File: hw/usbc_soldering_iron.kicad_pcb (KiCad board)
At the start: 4 copper layers, 100 x 13.5 mm, 91 parts, among them J1 U263-163N-4OS1735, J10 Conn_01x01, J11 Conn_01x01, J12 Conn_01x01, J13 Conn_01x01, J14 Conn_01x01, J15 Conn_01x01, J16 Conn_01x01, J17 Conn_01x01, J18 Conn_01x01, J19 Conn_01x01, J2 Conn_01x01, J20 Conn_01x01, J21 Conn_01x01, J22 Conn_01x01, J3 OLED, J4 Conn_01x01, J5 Conn_01x01, J6 Conn_01x01, J7 Conn_01x01, J8 Conn_01x01, J9 Conn_01x01, Q1 AGM403AP, SW1 SW_Push, U1 SC7A20, U10 TPA191Ax, U2 CH32X035F8U6, U3 TPD4E05U06DQA, U4 SIQ-02FVS3, U5 AP63203WU, U6 TLV333IDBVR, U8 MT3608, U9 IRS20752L, IRS20752L, NSG10752

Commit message: display
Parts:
- moved C14 12.9 mm to (116.7, 73.1), turned to 0 degrees
- moved J22 11.6 mm to (120.4, 78.5), turned to 0 degrees
- moved J19 9.21 mm to (118.9, 78.5), turned to 0 degrees
- moved C16 9.16 mm to (119.8, 73.1), turned to 0 degrees
- moved C20 7.42 mm to (116.7, 74.6), turned to 0 degrees
- moved J20 7.33 mm to (117.4, 78.5), turned to 0 degrees
- moved C18 7.28 mm to (116.7, 71.6)
- moved C22 7.18 mm to (116.7, 76.1), turned to 0 degrees
- moved J21 6.36 mm to (115.9, 78.5), turned to 0 degrees
- moved C17 5.81 mm to (119.8, 71.6), turned to 0 degrees
- moved R13 5.49 mm to (119.8, 76.1), turned to 0 degrees
- moved R12 4.86 mm to (119.8, 74.6)
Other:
- board size 100 x 13.5 mm -> 100 x 36.8 mm

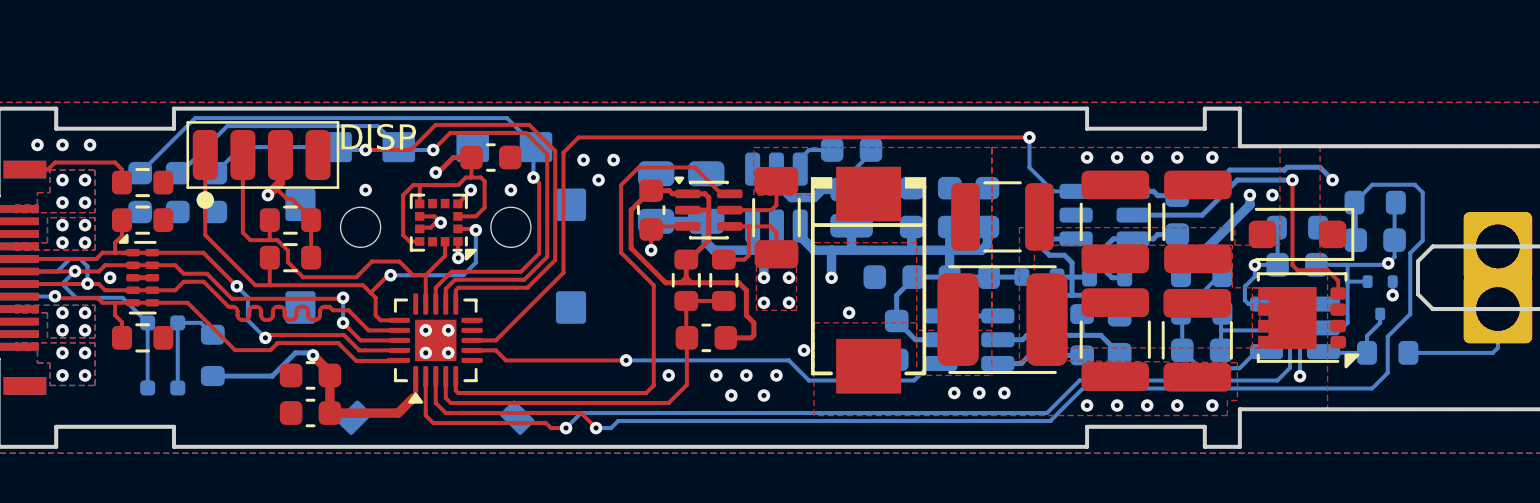
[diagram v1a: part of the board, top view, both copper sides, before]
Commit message: tlv333 rc filter
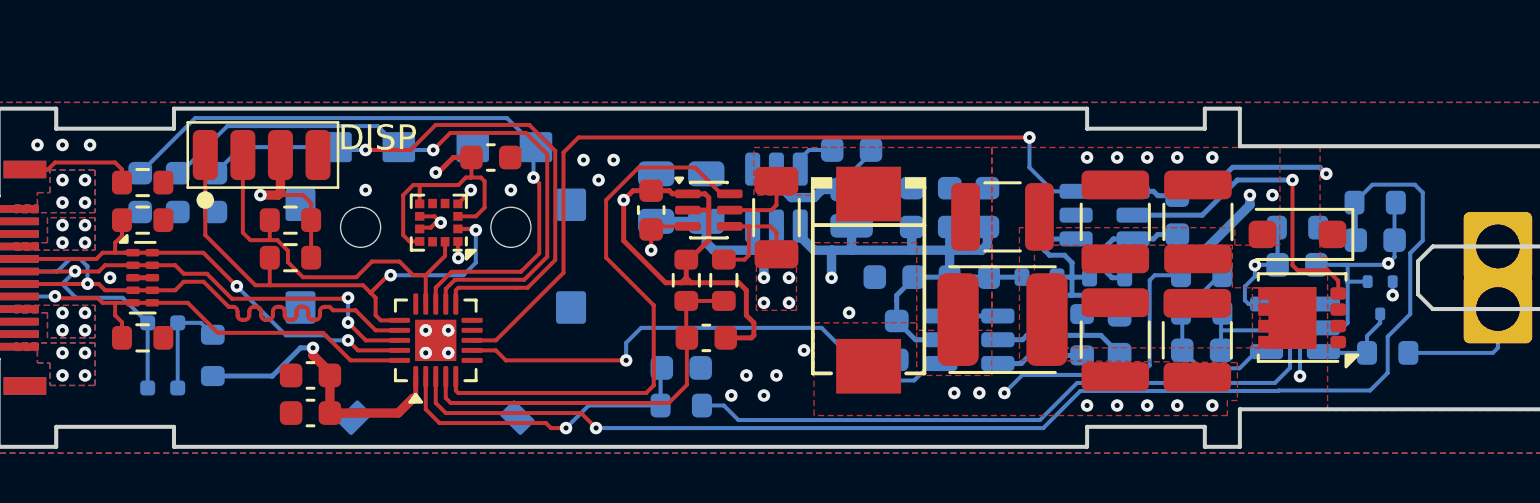
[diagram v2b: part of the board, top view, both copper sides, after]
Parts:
- added C33: TBD, Capacitor_SMD:C_0603_1608Metric, B.Cu at (132.7, 103.6)
- added R20: TBD, Resistor_SMD:R_0603_1608Metric, B.Cu at (132.7, 105.1)
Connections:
- C10 pad 2: /TC_FB -> Net-(C10-Pad2)
- R10 pad 2: /TC_FB -> Net-(C10-Pad2)
- U2 pad 9: /DISP_NRST -> /NRST
- U6 pad 1: /TC_FB -> Net-(C10-Pad2)
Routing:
- net Net-(C10-Pad2): track 0.00 -> 32.5 mm
- net /TC_FB: track 45.1 -> 12.9 mm
- net GND: track 45.4 -> 57.9 mm, vias 49 -> 48
- net +3.3V: track 112.6 -> 114.3 mm
- net /VDRIVE_ON: track 19.5 -> 21.0 mm
- net /CC1: track 19.3 -> 18.7 mm

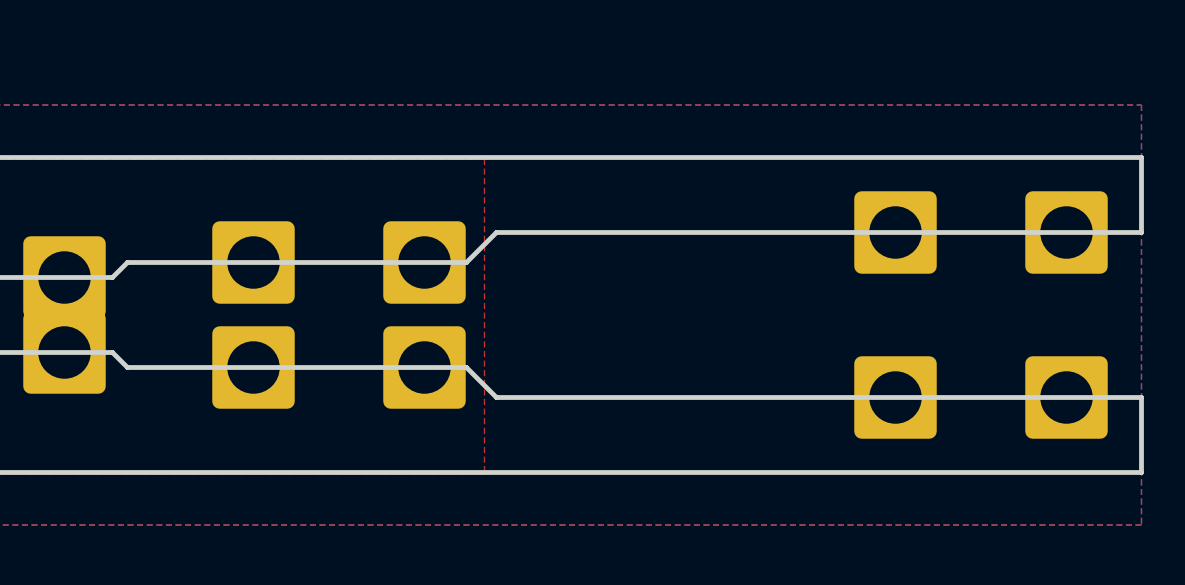
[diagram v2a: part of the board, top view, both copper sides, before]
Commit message: vias around tip contacts
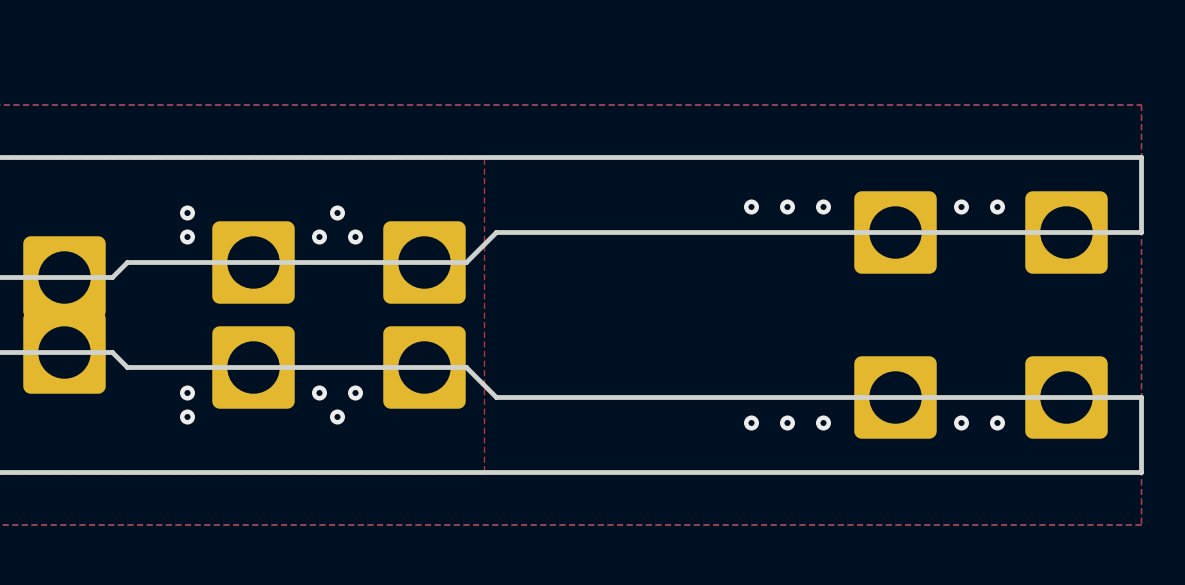
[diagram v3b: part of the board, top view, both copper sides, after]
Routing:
- net GND: vias 48 -> 58
- net /BLUE: vias 1 -> 11
- added copper zone on In1.Cu, net /BLUE
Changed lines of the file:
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@@
 	)
 	(via
+		(at 199 103.6)
+		(size 0.5)
+		(drill 0.2)
+		(layers "F.Cu" "B.Cu")
+		(free yes)
+		(net "GND")
+	)
+	(via
 		(at 151.3 95.2)
 		(size 0.5)
@@
 	)
 	(via
+		(at 192 103.6)
+		(size 0.5)
+		(drill 0.2)
+		(layers "F.Cu" "B.Cu")
+		(free yes)
+		(net "GND")
+	)
+	(via
 		(at 136 104.7)
 		(size 0.5)
@@
 	)
 	(via
+		(at 200.2 103.6)
+		(size 0.5)
+		(drill 0.2)
+		(layers "F.Cu" "B.Cu")
+		(free yes)
+		(net "GND")
+	)
+	(via
 		(at 144.6 104.6)
 		(size 0.5)
@@
 	)
 	(via
+		(at 199 96.4)
+		(size 0.5)
+		(drill 0.2)
+		(layers "F.Cu" "B.Cu")
+		(free yes)
+		(net "GND")
+	)
+	(via
 		(at 128.8 95.3)
 		(size 0.5)
@@
 	)
 	(via
+		(at 194.4 103.6)
+		(size 0.5)
+		(drill 0.2)
+		(layers "F.Cu" "B.Cu")
+		(free yes)
+		(net "GND")
+	)
+	(via
 		(at 145.6 104.6)
 		(size 0.5)
@@
 	)
 	(via
+		(at 193.2 103.6)
+		(size 0.5)
+		(drill 0.2)
+		(layers "F.Cu" "B.Cu")
+		(free yes)
+		(net "GND")
+	)
+	(via
 		(at 108.9 96.1)
 		(size 0.5)
@@
 	)
 	(via
+		(at 200.2 96.4)
+		(size 0.5)
+		(drill 0.2)
+		(layers "F.Cu" "B.Cu")
+		(free yes)
+		(net "GND")
+	)
+	(via
 		(at 123.4 103)
 		(size 0.5)
@@
 	)
 	(via
+		(at 193.2 96.4)
+		(size 0.5)
+		(drill 0.2)
+		(layers "F.Cu" "B.Cu")
+		(free yes)
+		(net "GND")
+	)
+	(via
 		(at 108.9 103.9)
 		(size 0.5)
@@
 	)
 	(via
+		(at 194.4 96.4)
+		(size 0.5)
+		(drill 0.2)
+		(layers "F.Cu" "B.Cu")
+		(free yes)
+		(net "GND")
+	)
+	(via
+		(at 192 96.4)
+		(size 0.5)
+		(drill 0.2)
+		(layers "F.Cu" "B.Cu")
+		(free yes)
+		(net "GND")
+	)
+	(via
 		(at 153.9 105.1)
 		(size 0.5)
@@
 		(net "/BLUE")
 	)
+	(via
+		(at 173.2 103.4)
+		(size 0.5)
+		(drill 0.2)
+		(layers "F.Cu" "B.Cu")
+		(free yes)
+		(net "/BLUE")
+	)
+	(via
+		(at 177.6 102.6)
+		(size 0.5)
+		(drill 0.2)
+		(layers "F.Cu" "B.Cu")
+		(free yes)
+		(net "/BLUE")
+	)
+	(via
+		(at 173.2 102.6)
+		(size 0.5)
+		(drill 0.2)
+		(layers "F.Cu" "B.Cu")
+		(free yes)
+		(net "/BLUE")
+	)
+	(via
+		(at 173.2 97.4)
+		(size 0.5)
+		(drill 0.2)
+		(layers "F.Cu" "B.Cu")
+		(free yes)
+		(net "/BLUE")
+	)
+	(via
+		(at 177.6 97.4)
+		(size 0.5)
+		(drill 0.2)
+		(layers "F.Cu" "B.Cu")
+		(free yes)
+		(net "/BLUE")
+	)
+	(via
+		(at 178.8 97.4)
+		(size 0.5)
+		(drill 0.2)
+		(layers "F.Cu" "B.Cu")
+		(free yes)
+		(net "/BLUE")
+	)
+	(via
+		(at 173.2 96.6)
+		(size 0.5)
+		(drill 0.2)
+		(layers "F.Cu" "B.Cu")
+		(free yes)
+		(net "/BLUE")
+	)
+	(via
+		(at 178.8 102.6)
+		(size 0.5)
+		(drill 0.2)
+		(layers "F.Cu" "B.Cu")
+		(free yes)
+		(net "/BLUE")
+	)
+	(via
+		(at 178.2 103.4)
+		(size 0.5)
+		(drill 0.2)
+		(layers "F.Cu" "B.Cu")
+		(free yes)
+		(net "/BLUE")
+	)
+	(via
+		(at 178.2 96.6)
+		(size 0.5)
+		(drill 0.2)
+		(layers "F.Cu" "B.Cu")
+		(free yes)
+		(net "/BLUE")
+	)
 	(segment
 		(start 158.19 95.59)
@@
 			)
 		)
+	)
+	(zone
+		(net "/BLUE")
+		(layer "In1.Cu")
+		(hatch edge 0.5)
+		(priority 11)
+		(connect_pads
+			(clearance 0.2)
+		)
+		(min_thickness 0.25)
+		(fill yes
+			(thermal_gap 0.3)
+			(thermal_bridge_width 1)
+			(island_removal_mode 0)
+		)
+		(polygon
+			(pts
+				(xy 172.6 95.6) (xy 182.4 95.6) (xy 182.4 104.4) (xy 172.6 104.4)
+			)
+		)

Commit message: oled board
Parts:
- added H1: MountingHole, MountingHole:MountingHole_2.2mm_M2_ISO7380, F.Cu at (114.6, 87.3)
- added H2: MountingHole, MountingHole:MountingHole_2.2mm_M2_ISO7380, F.Cu at (145.7, 87.3)
- J3: footprint Custom:FPC_14 -> Custom:X069-9616TSWIG02-H14
- moved C17 18.6 mm to (130.8, 86.7)
- moved C14 17.4 mm to (127.7, 86.7)
- moved C18 17.4 mm to (127.7, 85.2)
- moved C20 17.4 mm to (127.7, 88.2)
- moved C22 17.4 mm to (127.7, 89.7)
- moved R12 17.4 mm to (130.8, 88.2)
- moved R13 17.4 mm to (130.8, 89.7)
- moved J3 16.7 mm to (124.8, 87.4), turned to 180 degrees
- moved C16 16.3 mm to (130.8, 85.2)
- moved J19 13.0 mm to (123.7, 90.7)
- moved J20 13.0 mm to (122.2, 90.7)
- moved J21 13.0 mm to (120.7, 90.7)
- moved J22 13.0 mm to (125.2, 90.7)
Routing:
- net /DISP_VCC: track 0.00 -> 23.9 mm, vias 0 -> 2
- net Net-(J3-Pin_14): track 0.00 -> 19.0 mm, vias 0 -> 1
- net Net-(J3-Pin_13): track 0.00 -> 14.3 mm, vias 0 -> 1
- net Net-(J3-Pin_12): track 0.00 -> 14.1 mm, vias 0 -> 1
- net /DISP_NRST: track 0.00 -> 12.7 mm, vias 0 -> 1
- net Net-(J3-Pin_3): track 0.00 -> 11.3 mm, vias 0 -> 1
- net Net-(J3-Pin_1): track 0.00 -> 10.9 mm, vias 0 -> 1
- net /DISP_GND: track 0.00 -> 8.63 mm, vias 0 -> 7
- net Net-(J3-Pin_2): track 0.00 -> 6.97 mm, vias 0 -> 1
- net Net-(J3-Pin_4): track 0.00 -> 6.80 mm, vias 0 -> 1
- net /DISP_SDA: track 0.00 -> 5.13 mm, vias 0 -> 1
- net /DISP_SCL: track 0.00 -> 3.42 mm, vias 0 -> 1
- net +3.3V: track 114.3 -> 114.9 mm
- added copper zone on B.Cu, net /DISP_GND
- added copper zone on F.Cu, net /DISP_GND
- added copper zone on In1.Cu, net /DISP_GND
- added copper zone on In2.Cu, net /DISP_GND
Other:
- board size 100 x 36.8 mm -> 100 x 24 mm

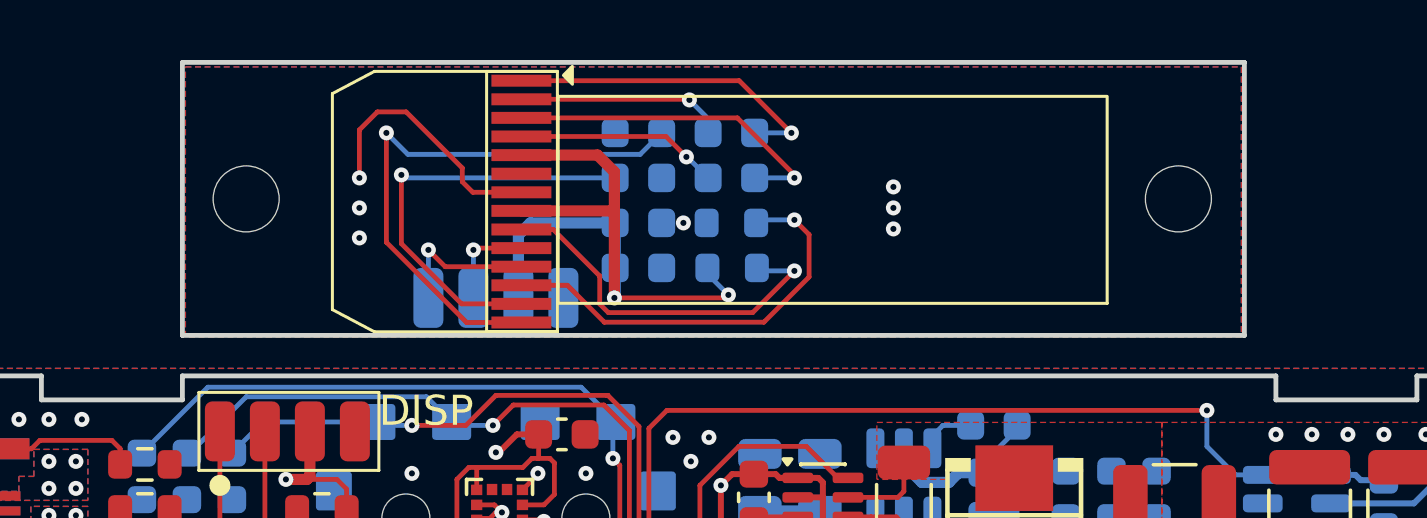
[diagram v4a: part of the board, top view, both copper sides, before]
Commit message: removed oled from main board
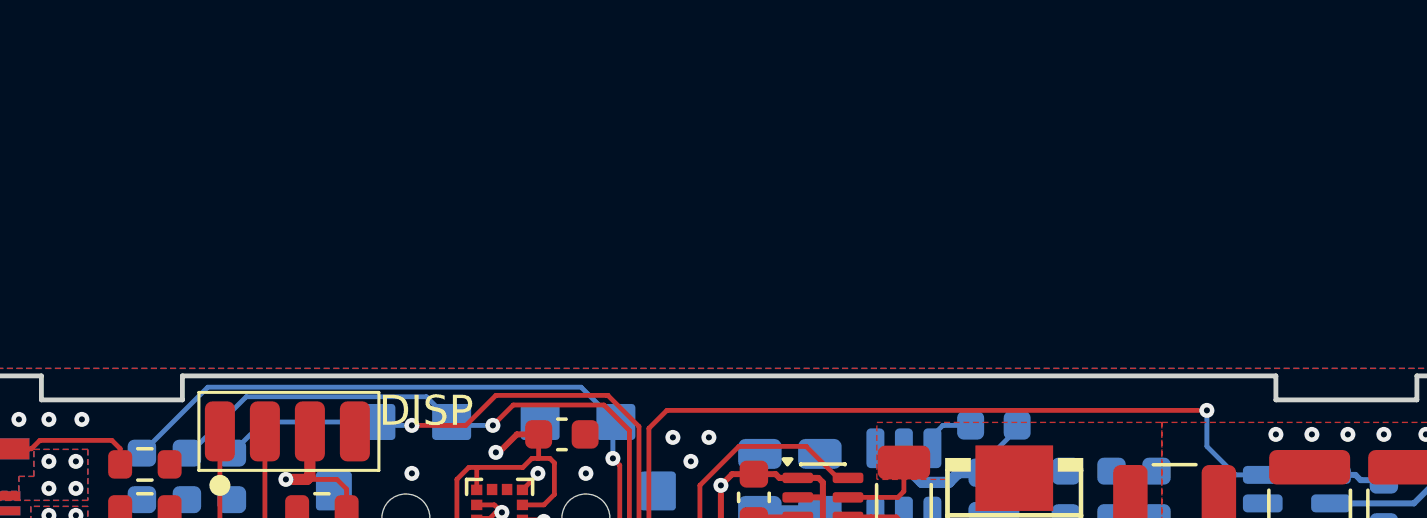
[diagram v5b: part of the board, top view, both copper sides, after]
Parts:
- removed C14, C20: 4.7u, Capacitor_SMD:C_0603_1608Metric
- removed C16, C17: 1u, Capacitor_SMD:C_0603_1608Metric
- removed C18, C22: 100n, Capacitor_SMD:C_0603_1608Metric
- removed H1, H2: MountingHole, MountingHole:MountingHole_2.2mm_M2_ISO7380
- removed J19, J20, J21, J22: Conn_01x01, Connector_Wire:SolderWirePad_1x01_SMD_1x2mm
- removed J3: OLED, Custom:X069-9616TSWIG02-H14
- removed R12: 560k, Resistor_SMD:R_0603_1608Metric
- removed R13: 1k, Resistor_SMD:R_0603_1608Metric
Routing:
- net /DISP_VCC: track 23.9 -> 0.00 mm, vias 2 -> 0
- net Net-(J3-Pin_14): track 19.0 -> 0.00 mm, vias 1 -> 0
- net Net-(J3-Pin_13): track 14.3 -> 0.00 mm, vias 1 -> 0
- net Net-(J3-Pin_12): track 14.1 -> 0.00 mm, vias 1 -> 0
- net /DISP_NRST: track 12.7 -> 0.00 mm, vias 1 -> 0
- net Net-(J3-Pin_3): track 11.3 -> 0.00 mm, vias 1 -> 0
- net Net-(J3-Pin_1): track 10.9 -> 0.00 mm, vias 1 -> 0
- net /DISP_GND: track 8.63 -> 0.00 mm, vias 7 -> 0
- net Net-(J3-Pin_2): track 6.97 -> 0.00 mm, vias 1 -> 0
- net Net-(J3-Pin_4): track 6.80 -> 0.00 mm, vias 1 -> 0
- net /DISP_SDA: track 5.13 -> 0.00 mm, vias 1 -> 0
- net /DISP_SCL: track 3.42 -> 0.00 mm, vias 1 -> 0
- removed copper zone on B.Cu, net /DISP_GND
- removed copper zone on F.Cu, net /DISP_GND
- removed copper zone on In1.Cu, net /DISP_GND
- removed copper zone on In2.Cu, net /DISP_GND
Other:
- board size 100 x 24 mm -> 100 x 13.5 mm

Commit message: 3d files and oled board
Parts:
- added TP1: TestPoint, TestPoint:TestPoint_Pad_D1.0mm, F.Cu at (128.5, 101.3)
- added TP2: TestPoint, TestPoint:TestPoint_Pad_D1.0mm, F.Cu at (126.5, 101.3)
- moved C26 0.20 mm to (152.5, 97.3)
- moved U9 0.20 mm to (149.6, 97.3)
- moved C12 0.10 mm to (131.4, 97.3)
- moved L1 0.10 mm to (139.6, 97.2)
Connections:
- U1 pad 6: unconnected-(U1-INT2-Pad6) -> /ACC_INT
- U2 pad 15: /PB12 -> /ACC_INT
- U2 pad 6: /PA4 -> unconnected-(U2-PA4-Pad6)
- U2 pad 9: /NRST -> /PA7
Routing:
- net /ACC_INT: track 0.00 -> 10.1 mm, vias 0 -> 2
- net /PA7: track 0.00 -> 4.48 mm
- net /HEATER_ON: track 31.9 -> 35.3 mm
- net /PB0: track 0.00 -> 2.32 mm
- net +3.3V: track 114.9 -> 116.0 mm

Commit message: minor touch-ups on PCB
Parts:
- removed J18: Conn_01x01, Connector_Wire:SolderWirePad_1x01_SMD_1x2mm
- added J3: Conn_01x01, Connector_Wire:SolderWirePad_1x01_SMD_1x2mm, F.Cu at (115.2, 95.1)
- C33: value TBD -> 15n CG0
- R20: value TBD -> 1k
- moved J4 1.50 mm to (116.7, 95.1)
- moved J5 1.50 mm to (118.2, 95.1)
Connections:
- J4 pad 1: /SCL -> +3.3V
- J5 pad 1: +3.3V -> GND
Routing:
- net /VTIP: track 0.00 -> 9.91 mm
- net +3.3V: track 116.0 -> 119.8 mm
- net GND: vias 58 -> 61

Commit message: silkscreen and better contacts
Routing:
- net GND: track 58.1 -> 101.7 mm
- net /BLUE: track 8.36 -> 51.1 mm
- added copper zone on B.Cu, net /BLUE
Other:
- board text added: "USB-C Soldering Iron v0.2"
